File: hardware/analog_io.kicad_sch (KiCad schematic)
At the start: 40 parts, among them J24 AI0/GND/AI1/GND/AI2/GND, J25 0-10 V outputs 0-3; pin 1 = c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, U37 L78L12ACUTR, U38 TLV2374IDR

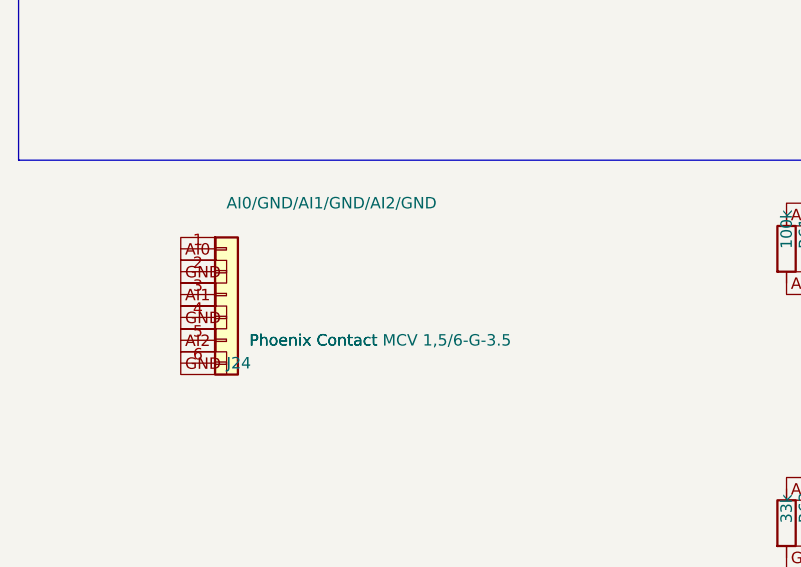
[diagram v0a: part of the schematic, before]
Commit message: Update RP2350B PCB, pinout and fabrication rules
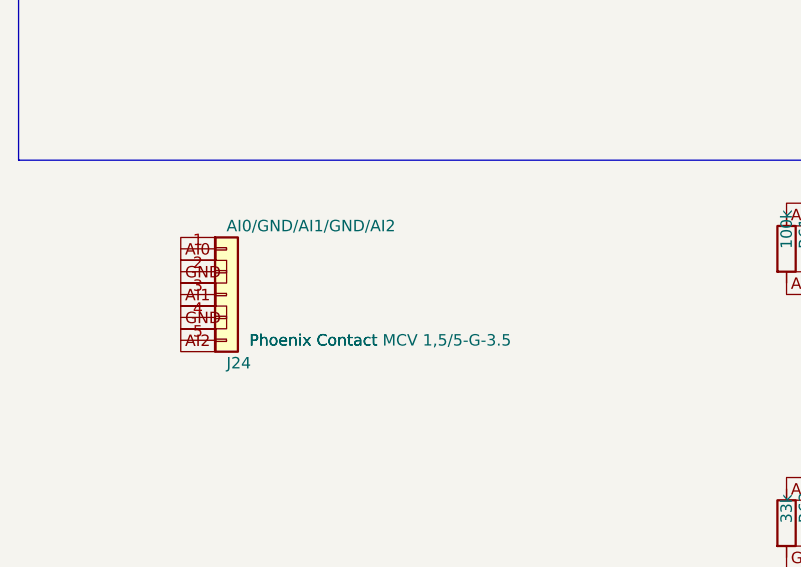
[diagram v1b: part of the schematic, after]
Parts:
- removed J24: AI0/GND/AI1/GND/AI2/GND, Connector_Phoenix_MC:PhoenixContact_MCV_1,5_6-G-3.5_1x06_P3.50mm_Vertical, symbol Connector_Generic:Conn_01x06
- added J24: AI0/GND/AI1/GND/AI2, Connector_Phoenix_MC:PhoenixContact_MCV_1,5_5-G-3.5_1x05_P3.50mm_Vertical, symbol Connector_Generic:Conn_01x05
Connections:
- net AI0: now also J24.1 (Pin_1)
- net AI1: now also J24.3 (Pin_3)
- net AI2: now also J24.5 (Pin_5)
- net GND: now also J24.2 (Pin_2), J24.4 (Pin_4)
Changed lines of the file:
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@@
 	)
 	(symbol
-		(lib_id "Connector_Generic:Conn_01x06")
+		(lib_id "Connector_Generic:Conn_01x05")
 		(at 38.1 74.93 0)
 		(unit 1)
@@
 			)
 		)
-		(property "Value" "AI0/GND/AI1/GND/AI2/GND"
-			(at 38.1 64.77 0.0000)
-			(effects
-				(font
-					(size 1.27 1.27)
-				)
-				(justify left)
-			)
-		)
-		(property "Footprint" "Connector_Phoenix_MC:PhoenixContact_MCV_1,5_6-G-3.5_1x06_P3.50mm_Vertical"
+		(property "Value" "AI0/GND/AI1/GND/AI2"
+			(at 38.1 67.31 0.0000)
+			(effects
+				(font
+					(size 1.27 1.27)
+				)
+				(justify left)
+			)
+		)
+		(property "Footprint" "Connector_Phoenix_MC:PhoenixContact_MCV_1,5_5-G-3.5_1x05_P3.50mm_Vertical"
 			(at 38.1 74.93 0.0000)
 			(effects
@@
 			)
 		)
-		(property "MPN" "Phoenix Contact MCV 1,5/6-G-3.5"
+		(property "MPN" "Phoenix Contact MCV 1,5/5-G-3.5"
 			(at 40.64 80.0099 0)
 			(effects
@@
 		(pin "5"
 		)
-		(pin "6"
-		)
-		(instances
-			(project "Analog I/O"
-				(path "/b987e4d8-86ae-42ec-9f4b-ba173e7be2d1"
+		(instances
+			(project "Analog I/O"
+				(path "/37287d9f-c20d-46ea-aa33-355b2f36a559"
 					(reference "J24")
 					(unit 1)
@@
 		(instances
 			(project "Analog I/O"
-				(path "/b987e4d8-86ae-42ec-9f4b-ba173e7be2d1"
+				(path "/37287d9f-c20d-46ea-aa33-355b2f36a559"
 					(reference "R61")
 					(unit 1)
@@
 		(instances
 			(project "Analog I/O"
-				(path "/b987e4d8-86ae-42ec-9f4b-ba173e7be2d1"
+				(path "/37287d9f-c20d-46ea-aa33-355b2f36a559"
 					(reference "R63")
 					(unit 1)
@@
 		(instances
 			(project "Analog I/O"
-				(path "/b987e4d8-86ae-42ec-9f4b-ba173e7be2d1"
+				(path "/37287d9f-c20d-46ea-aa33-355b2f36a559"
 					(reference "C73")
 					(unit 1)
@@
 		(instances
 			(project "Analog I/O"
-				(path "/b987e4d8-86ae-42ec-9f4b-ba173e7be2d1"
+				(path "/37287d9f-c20d-46ea-aa33-355b2f36a559"
 					(reference "R64")
 					(unit 1)
@@
 		(instances
 			(project "Analog I/O"
-				(path "/b987e4d8-86ae-42ec-9f4b-ba173e7be2d1"
+				(path "/37287d9f-c20d-46ea-aa33-355b2f36a559"
 					(reference "R66")
 					(unit 1)
@@
 		(instances
 			(project "Analog I/O"
-				(path "/b987e4d8-86ae-42ec-9f4b-ba173e7be2d1"
+				(path "/37287d9f-c20d-46ea-aa33-355b2f36a559"
 					(reference "C74")
 					(unit 1)
@@
 		(instances
 			(project "Analog I/O"
-				(path "/b987e4d8-86ae-42ec-9f4b-ba173e7be2d1"
+				(path "/37287d9f-c20d-46ea-aa33-355b2f36a559"
 					(reference "R67")
 					(unit 1)
@@
 		(instances
 			(project "Analog I/O"
-				(path "/b987e4d8-86ae-42ec-9f4b-ba173e7be2d1"
+				(path "/37287d9f-c20d-46ea-aa33-355b2f36a559"
 					(reference "R69")
 					(unit 1)
@@
 		(instances
 			(project "Analog I/O"
-				(path "/b987e4d8-86ae-42ec-9f4b-ba173e7be2d1"
+				(path "/37287d9f-c20d-46ea-aa33-355b2f36a559"
 					(reference "C75")
 					(unit 1)
@@
 		(instances
 			(project "Analog I/O"
-				(path "/b987e4d8-86ae-42ec-9f4b-ba173e7be2d1"
+				(path "/37287d9f-c20d-46ea-aa33-355b2f36a559"
 					(reference "J25")
 					(unit 1)
@@
 		(instances
 			(project "Analog I/O"
-				(path "/b987e4d8-86ae-42ec-9f4b-ba173e7be2d1"
+				(path "/37287d9f-c20d-46ea-aa33-355b2f36a559"
 					(reference "R92")
 					(unit 1)
@@
 		(instances
 			(project "Analog I/O"
-				(path "/b987e4d8-86ae-42ec-9f4b-ba173e7be2d1"
+				(path "/37287d9f-c20d-46ea-aa33-355b2f36a559"
 					(reference "R96")
 					(unit 1)
@@
 		(instances
 			(project "Analog I/O"
-				(path "/b987e4d8-86ae-42ec-9f4b-ba173e7be2d1"
+				(path "/37287d9f-c20d-46ea-aa33-355b2f36a559"
 					(reference "R100")
 					(unit 1)
@@
 		(instances
 			(project "Analog I/O"
-				(path "/b987e4d8-86ae-42ec-9f4b-ba173e7be2d1"
+				(path "/37287d9f-c20d-46ea-aa33-355b2f36a559"
 					(reference "R104")
 					(unit 1)
@@
 		(instances
 			(project "Analog I/O"
-				(path "/b987e4d8-86ae-42ec-9f4b-ba173e7be2d1"
+				(path "/37287d9f-c20d-46ea-aa33-355b2f36a559"
 					(reference "R93")
 					(unit 1)
@@
 		(instances
 			(project "Analog I/O"
-				(path "/b987e4d8-86ae-42ec-9f4b-ba173e7be2d1"
+				(path "/37287d9f-c20d-46ea-aa33-355b2f36a559"
 					(reference "R97")
 					(unit 1)
@@
 		(instances
 			(project "Analog I/O"
-				(path "/b987e4d8-86ae-42ec-9f4b-ba173e7be2d1"
+				(path "/37287d9f-c20d-46ea-aa33-355b2f36a559"
 					(reference "R101")
 					(unit 1)
@@
 		(instances
 			(project "Analog I/O"
-				(path "/b987e4d8-86ae-42ec-9f4b-ba173e7be2d1"
+				(path "/37287d9f-c20d-46ea-aa33-355b2f36a559"
 					(reference "R105")
 					(unit 1)
@@
 		(instances
 			(project "Analog I/O"
-				(path "/b987e4d8-86ae-42ec-9f4b-ba173e7be2d1"
+				(path "/37287d9f-c20d-46ea-aa33-355b2f36a559"
 					(reference "R94")
 					(unit 1)
@@
 		(instances
 			(project "Analog I/O"
-				(path "/b987e4d8-86ae-42ec-9f4b-ba173e7be2d1"
+				(path "/37287d9f-c20d-46ea-aa33-355b2f36a559"
 					(reference "R98")
 					(unit 1)
@@
 		(instances
 			(project "Analog I/O"
-				(path "/b987e4d8-86ae-42ec-9f4b-ba173e7be2d1"
+				(path "/37287d9f-c20d-46ea-aa33-355b2f36a559"
 					(reference "R102")
 					(unit 1)
@@
 		(instances
 			(project "Analog I/O"
-				(path "/b987e4d8-86ae-42ec-9f4b-ba173e7be2d1"
+				(path "/37287d9f-c20d-46ea-aa33-355b2f36a559"
 					(reference "R106")
 					(unit 1)
@@
 		(instances
 			(project "Analog I/O"
-				(path "/b987e4d8-86ae-42ec-9f4b-ba173e7be2d1"
+				(path "/37287d9f-c20d-46ea-aa33-355b2f36a559"
 					(reference "R95")
 					(unit 1)
@@
 		(instances
 			(project "Analog I/O"
-				(path "/b987e4d8-86ae-42ec-9f4b-ba173e7be2d1"
+				(path "/37287d9f-c20d-46ea-aa33-355b2f36a559"
 					(reference "R99")
 					(unit 1)
@@
 		(instances
 			(project "Analog I/O"
-				(path "/b987e4d8-86ae-42ec-9f4b-ba173e7be2d1"
+				(path "/37287d9f-c20d-46ea-aa33-355b2f36a559"
 					(reference "R103")
 					(unit 1)
@@
 		(instances
 			(project "Analog I/O"
-				(path "/b987e4d8-86ae-42ec-9f4b-ba173e7be2d1"
+				(path "/37287d9f-c20d-46ea-aa33-355b2f36a559"
 					(reference "R107")
 					(unit 1)
@@
 		(instances
 			(project "Analog I/O"
-				(path "/b987e4d8-86ae-42ec-9f4b-ba173e7be2d1"
+				(path "/37287d9f-c20d-46ea-aa33-355b2f36a559"
 					(reference "C92")
 					(unit 1)
@@
 		(instances
 			(project "Analog I/O"
-				(path "/b987e4d8-86ae-42ec-9f4b-ba173e7be2d1"
+				(path "/37287d9f-c20d-46ea-aa33-355b2f36a559"
 					(reference "C93")
 					(unit 1)
@@
 		(instances
 			(project "Analog I/O"
-				(path "/b987e4d8-86ae-42ec-9f4b-ba173e7be2d1"
+				(path "/37287d9f-c20d-46ea-aa33-355b2f36a559"
 					(reference "C94")
 					(unit 1)
@@
 		(instances
 			(project "Analog I/O"
-				(path "/b987e4d8-86ae-42ec-9f4b-ba173e7be2d1"
+				(path "/37287d9f-c20d-46ea-aa33-355b2f36a559"
 					(reference "C95")
 					(unit 1)
@@
 		(instances
 			(project "Analog I/O"
-				(path "/b987e4d8-86ae-42ec-9f4b-ba173e7be2d1"
+				(path "/37287d9f-c20d-46ea-aa33-355b2f36a559"
 					(reference "C96")
 					(unit 1)
@@
 		(instances
 			(project "Analog I/O"
-				(path "/b987e4d8-86ae-42ec-9f4b-ba173e7be2d1"
+				(path "/37287d9f-c20d-46ea-aa33-355b2f36a559"
 					(reference "C97")
 					(unit 1)
@@
 		(instances
 			(project "Analog I/O"
-				(path "/b987e4d8-86ae-42ec-9f4b-ba173e7be2d1"
+				(path "/37287d9f-c20d-46ea-aa33-355b2f36a559"
 					(reference "C98")
 					(unit 1)
@@
 		(instances
 			(project "Analog I/O"
-				(path "/b987e4d8-86ae-42ec-9f4b-ba173e7be2d1"
+				(path "/37287d9f-c20d-46ea-aa33-355b2f36a559"
 					(reference "C99")
 					(unit 1)
@@
 		(instances
 			(project "Analog I/O"
-				(path "/b987e4d8-86ae-42ec-9f4b-ba173e7be2d1"
+				(path "/37287d9f-c20d-46ea-aa33-355b2f36a559"
 					(reference "U38")
 					(unit 1)
@@
 		(instances
 			(project "Analog I/O"
-				(path "/b987e4d8-86ae-42ec-9f4b-ba173e7be2d1"
+				(path "/37287d9f-c20d-46ea-aa33-355b2f36a559"
 					(reference "U37")
 					(unit 1)
@@
 		(instances
 			(project "Analog I/O"
-				(path "/b987e4d8-86ae-42ec-9f4b-ba173e7be2d1"
+				(path "/37287d9f-c20d-46ea-aa33-355b2f36a559"
 					(reference "C100")
 					(unit 1)
@@
 		(instances
 			(project "Analog I/O"
-				(path "/b987e4d8-86ae-42ec-9f4b-ba173e7be2d1"
+				(path "/37287d9f-c20d-46ea-aa33-355b2f36a559"
 					(reference "C101")
 					(unit 1)
@@
 		(instances
 			(project "Analog I/O"
-				(path "/b987e4d8-86ae-42ec-9f4b-ba173e7be2d1"
+				(path "/37287d9f-c20d-46ea-aa33-355b2f36a559"
 					(reference "C102")
 					(unit 1)
@@
 		(fields_autoplaced yes)
 		(effects
-			(font
-				(size 1.27 1.27)
-			)
-			(justify left bottom)
-		)
-	)
-	(global_label "GND"
-		(shape passive)
-		(at 33.02 82.55 0.0000)
-		(fields_autoplaced yes)
-		(effects

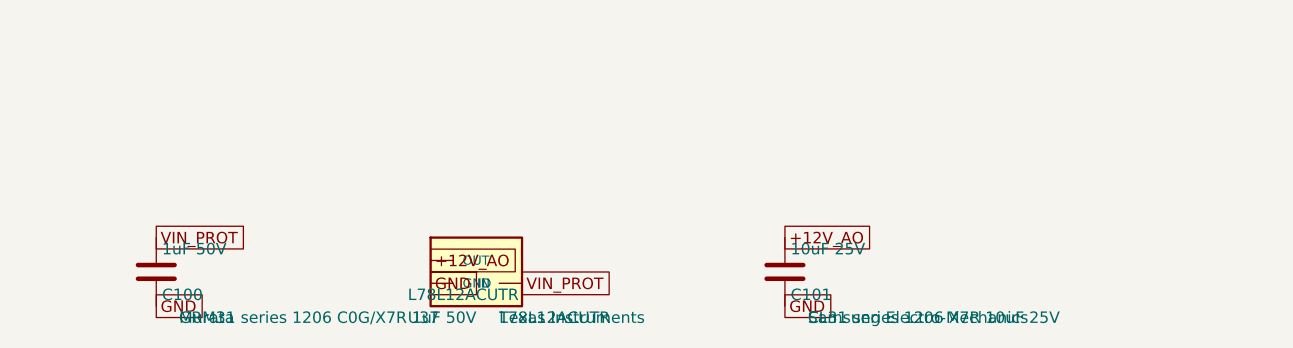
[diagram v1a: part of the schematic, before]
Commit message: Update RP2350 board power and I/O design
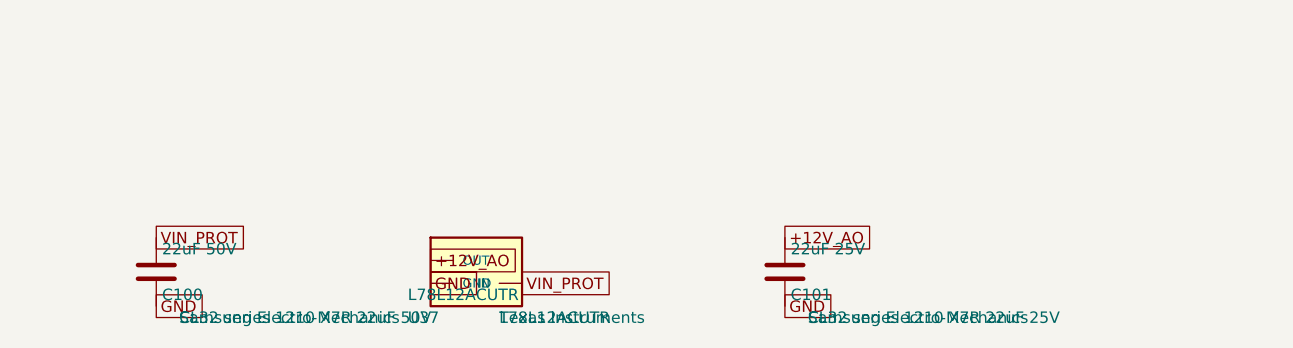
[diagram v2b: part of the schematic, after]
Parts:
- C100: value 1uF 50V -> 22uF 50V; footprint Capacitor_SMD:C_1206_3216Metric -> Capacitor_SMD:C_1210_3225Metric; MPN GRM31 series 1206 C0G/X7R 1uF 50V -> CL32 series 1210 X7R 22uF 50V; Manufacturer Murata -> Samsung Electro-Mechanics
- C101: value 10uF 25V -> 22uF 25V; footprint Capacitor_SMD:C_1206_3216Metric -> Capacitor_SMD:C_1210_3225Metric; MPN CL31 series 1206 X7R 10uF 25V -> CL32 series 1210 X7R 22uF 25V
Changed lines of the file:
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@@
 		(instances
 			(project "Analog I/O"
-				(path "/37287d9f-c20d-46ea-aa33-355b2f36a559"
+				(path "/7556d853-629e-4a43-b2a7-51d3b1a45efc"
 					(reference "J24")
 					(unit 1)
@@
 		(instances
 			(project "Analog I/O"
-				(path "/37287d9f-c20d-46ea-aa33-355b2f36a559"
+				(path "/7556d853-629e-4a43-b2a7-51d3b1a45efc"
 					(reference "R61")
 					(unit 1)
@@
 		(instances
 			(project "Analog I/O"
-				(path "/37287d9f-c20d-46ea-aa33-355b2f36a559"
+				(path "/7556d853-629e-4a43-b2a7-51d3b1a45efc"
 					(reference "R63")
 					(unit 1)
@@
 		(instances
 			(project "Analog I/O"
-				(path "/37287d9f-c20d-46ea-aa33-355b2f36a559"
+				(path "/7556d853-629e-4a43-b2a7-51d3b1a45efc"
 					(reference "C73")
 					(unit 1)
@@
 		(instances
 			(project "Analog I/O"
-				(path "/37287d9f-c20d-46ea-aa33-355b2f36a559"
+				(path "/7556d853-629e-4a43-b2a7-51d3b1a45efc"
 					(reference "R64")
 					(unit 1)
@@
 		(instances
 			(project "Analog I/O"
-				(path "/37287d9f-c20d-46ea-aa33-355b2f36a559"
+				(path "/7556d853-629e-4a43-b2a7-51d3b1a45efc"
 					(reference "R66")
 					(unit 1)
@@
 		(instances
 			(project "Analog I/O"
-				(path "/37287d9f-c20d-46ea-aa33-355b2f36a559"
+				(path "/7556d853-629e-4a43-b2a7-51d3b1a45efc"
 					(reference "C74")
 					(unit 1)
@@
 		(instances
 			(project "Analog I/O"
-				(path "/37287d9f-c20d-46ea-aa33-355b2f36a559"
+				(path "/7556d853-629e-4a43-b2a7-51d3b1a45efc"
 					(reference "R67")
 					(unit 1)
@@
 		(instances
 			(project "Analog I/O"
-				(path "/37287d9f-c20d-46ea-aa33-355b2f36a559"
+				(path "/7556d853-629e-4a43-b2a7-51d3b1a45efc"
 					(reference "R69")
 					(unit 1)
@@
 		(instances
 			(project "Analog I/O"
-				(path "/37287d9f-c20d-46ea-aa33-355b2f36a559"
+				(path "/7556d853-629e-4a43-b2a7-51d3b1a45efc"
 					(reference "C75")
 					(unit 1)
@@
 		(instances
 			(project "Analog I/O"
-				(path "/37287d9f-c20d-46ea-aa33-355b2f36a559"
+				(path "/7556d853-629e-4a43-b2a7-51d3b1a45efc"
 					(reference "J25")
 					(unit 1)
@@
 		(instances
 			(project "Analog I/O"
-				(path "/37287d9f-c20d-46ea-aa33-355b2f36a559"
+				(path "/7556d853-629e-4a43-b2a7-51d3b1a45efc"
 					(reference "R92")
 					(unit 1)
@@
 		(instances
 			(project "Analog I/O"
-				(path "/37287d9f-c20d-46ea-aa33-355b2f36a559"
+				(path "/7556d853-629e-4a43-b2a7-51d3b1a45efc"
 					(reference "R96")
 					(unit 1)
@@
 		(instances
 			(project "Analog I/O"
-				(path "/37287d9f-c20d-46ea-aa33-355b2f36a559"
+				(path "/7556d853-629e-4a43-b2a7-51d3b1a45efc"
 					(reference "R100")
 					(unit 1)
@@
 		(instances
 			(project "Analog I/O"
-				(path "/37287d9f-c20d-46ea-aa33-355b2f36a559"
+				(path "/7556d853-629e-4a43-b2a7-51d3b1a45efc"
 					(reference "R104")
 					(unit 1)
@@
 		(instances
 			(project "Analog I/O"
-				(path "/37287d9f-c20d-46ea-aa33-355b2f36a559"
+				(path "/7556d853-629e-4a43-b2a7-51d3b1a45efc"
 					(reference "R93")
 					(unit 1)
@@
 		(instances
 			(project "Analog I/O"
-				(path "/37287d9f-c20d-46ea-aa33-355b2f36a559"
+				(path "/7556d853-629e-4a43-b2a7-51d3b1a45efc"
 					(reference "R97")
 					(unit 1)
@@
 		(instances
 			(project "Analog I/O"
-				(path "/37287d9f-c20d-46ea-aa33-355b2f36a559"
+				(path "/7556d853-629e-4a43-b2a7-51d3b1a45efc"
 					(reference "R101")
 					(unit 1)
@@
 		(instances
 			(project "Analog I/O"
-				(path "/37287d9f-c20d-46ea-aa33-355b2f36a559"
+				(path "/7556d853-629e-4a43-b2a7-51d3b1a45efc"
 					(reference "R105")
 					(unit 1)
@@
 		(instances
 			(project "Analog I/O"
-				(path "/37287d9f-c20d-46ea-aa33-355b2f36a559"
+				(path "/7556d853-629e-4a43-b2a7-51d3b1a45efc"
 					(reference "R94")
 					(unit 1)
@@
 		(instances
 			(project "Analog I/O"
-				(path "/37287d9f-c20d-46ea-aa33-355b2f36a559"
+				(path "/7556d853-629e-4a43-b2a7-51d3b1a45efc"
 					(reference "R98")
 					(unit 1)
@@
 		(instances
 			(project "Analog I/O"
-				(path "/37287d9f-c20d-46ea-aa33-355b2f36a559"
+				(path "/7556d853-629e-4a43-b2a7-51d3b1a45efc"
 					(reference "R102")
 					(unit 1)
@@
 		(instances
 			(project "Analog I/O"
-				(path "/37287d9f-c20d-46ea-aa33-355b2f36a559"
+				(path "/7556d853-629e-4a43-b2a7-51d3b1a45efc"
 					(reference "R106")
 					(unit 1)
@@
 		(instances
 			(project "Analog I/O"
-				(path "/37287d9f-c20d-46ea-aa33-355b2f36a559"
+				(path "/7556d853-629e-4a43-b2a7-51d3b1a45efc"
 					(reference "R95")
 					(unit 1)
@@
 		(instances
 			(project "Analog I/O"
-				(path "/37287d9f-c20d-46ea-aa33-355b2f36a559"
+				(path "/7556d853-629e-4a43-b2a7-51d3b1a45efc"
 					(reference "R99")
 					(unit 1)
@@
 		(instances
 			(project "Analog I/O"
-				(path "/37287d9f-c20d-46ea-aa33-355b2f36a559"
+				(path "/7556d853-629e-4a43-b2a7-51d3b1a45efc"
 					(reference "R103")
 					(unit 1)
@@
 		(instances
 			(project "Analog I/O"
-				(path "/37287d9f-c20d-46ea-aa33-355b2f36a559"
+				(path "/7556d853-629e-4a43-b2a7-51d3b1a45efc"
 					(reference "R107")
 					(unit 1)
@@
 		(instances
 			(project "Analog I/O"
-				(path "/37287d9f-c20d-46ea-aa33-355b2f36a559"
+				(path "/7556d853-629e-4a43-b2a7-51d3b1a45efc"
 					(reference "C92")
 					(unit 1)
@@
 		(instances
 			(project "Analog I/O"
-				(path "/37287d9f-c20d-46ea-aa33-355b2f36a559"
+				(path "/7556d853-629e-4a43-b2a7-51d3b1a45efc"
 					(reference "C93")
 					(unit 1)
@@
 		(instances
 			(project "Analog I/O"
-				(path "/37287d9f-c20d-46ea-aa33-355b2f36a559"
+				(path "/7556d853-629e-4a43-b2a7-51d3b1a45efc"
 					(reference "C94")
 					(unit 1)
@@
 		(instances
 			(project "Analog I/O"
-				(path "/37287d9f-c20d-46ea-aa33-355b2f36a559"
+				(path "/7556d853-629e-4a43-b2a7-51d3b1a45efc"
 					(reference "C95")
 					(unit 1)
@@
 		(instances
 			(project "Analog I/O"
-				(path "/37287d9f-c20d-46ea-aa33-355b2f36a559"
+				(path "/7556d853-629e-4a43-b2a7-51d3b1a45efc"
 					(reference "C96")
 					(unit 1)
@@
 		(instances
 			(project "Analog I/O"
-				(path "/37287d9f-c20d-46ea-aa33-355b2f36a559"
+				(path "/7556d853-629e-4a43-b2a7-51d3b1a45efc"
 					(reference "C97")
 					(unit 1)
@@
 		(instances
 			(project "Analog I/O"
-				(path "/37287d9f-c20d-46ea-aa33-355b2f36a559"
+				(path "/7556d853-629e-4a43-b2a7-51d3b1a45efc"
 					(reference "C98")
 					(unit 1)
@@
 		(instances
 			(project "Analog I/O"
-				(path "/37287d9f-c20d-46ea-aa33-355b2f36a559"
+				(path "/7556d853-629e-4a43-b2a7-51d3b1a45efc"
 					(reference "C99")
 					(unit 1)
@@
 		(instances
 			(project "Analog I/O"
-				(path "/37287d9f-c20d-46ea-aa33-355b2f36a559"
+				(path "/7556d853-629e-4a43-b2a7-51d3b1a45efc"
 					(reference "U38")
 					(unit 1)
@@
 		(instances
 			(project "Analog I/O"
-				(path "/37287d9f-c20d-46ea-aa33-355b2f36a559"
+				(path "/7556d853-629e-4a43-b2a7-51d3b1a45efc"
 					(reference "U37")
 					(unit 1)
@@
 			)
 		)
-		(property "Value" "1uF 50V"
+		(property "Value" "22uF 50V"
 			(at 315.595 292.1 0.0000)
 			(effects
@@
 			)
 		)
-		(property "Footprint" "Capacitor_SMD:C_1206_3216Metric"
+		(property "Footprint" "Capacitor_SMD:C_1210_3225Metric"
 			(at 315.9252 290.83 0.0000)
 			(effects
@@
 			)
 		)
-		(property "MPN" "GRM31 series 1206 C0G/X7R 1uF 50V"
+		(property "MPN" "CL32 series 1210 X7R 22uF 50V"
 			(at 317.5 299.7199 0)
 			(effects
@@
 			)
 		)
-		(property "Manufacturer" "Murata"
+		(property "Manufacturer" "Samsung Electro-Mechanics"
 			(at 317.5 299.7199 0)
 			(effects
@@
 		(instances
 			(project "Analog I/O"
-				(path "/37287d9f-c20d-46ea-aa33-355b2f36a559"
+				(path "/7556d853-629e-4a43-b2a7-51d3b1a45efc"
 					(reference "C100")
 					(unit 1)
@@
 			)
 		)
-		(property "Value" "10uF 25V"
+		(property "Value" "22uF 25V"
 			(at 385.445 292.1 0.0000)
 			(effects
@@
 			)
 		)
-		(property "Footprint" "Capacitor_SMD:C_1206_3216Metric"
+		(property "Footprint" "Capacitor_SMD:C_1210_3225Metric"
 			(at 385.7752 290.83 0.0000)
 			(effects
@@
 			)
 		)
-		(property "MPN" "CL31 series 1206 X7R 10uF 25V"
+		(property "MPN" "CL32 series 1210 X7R 22uF 25V"
 			(at 387.35 299.7199 0)
 			(effects
@@
 		(instances
 			(project "Analog I/O"
-				(path "/37287d9f-c20d-46ea-aa33-355b2f36a559"
+				(path "/7556d853-629e-4a43-b2a7-51d3b1a45efc"
 					(reference "C101")
 					(unit 1)
@@
 		(instances
 			(project "Analog I/O"
-				(path "/37287d9f-c20d-46ea-aa33-355b2f36a559"
+				(path "/7556d853-629e-4a43-b2a7-51d3b1a45efc"
 					(reference "C102")
 					(unit 1)
